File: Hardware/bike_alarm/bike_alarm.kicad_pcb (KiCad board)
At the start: 2 copper layers, 4 parts, among them Q1 Q_NMOS_DGS, Y1 Piezo Buzzer

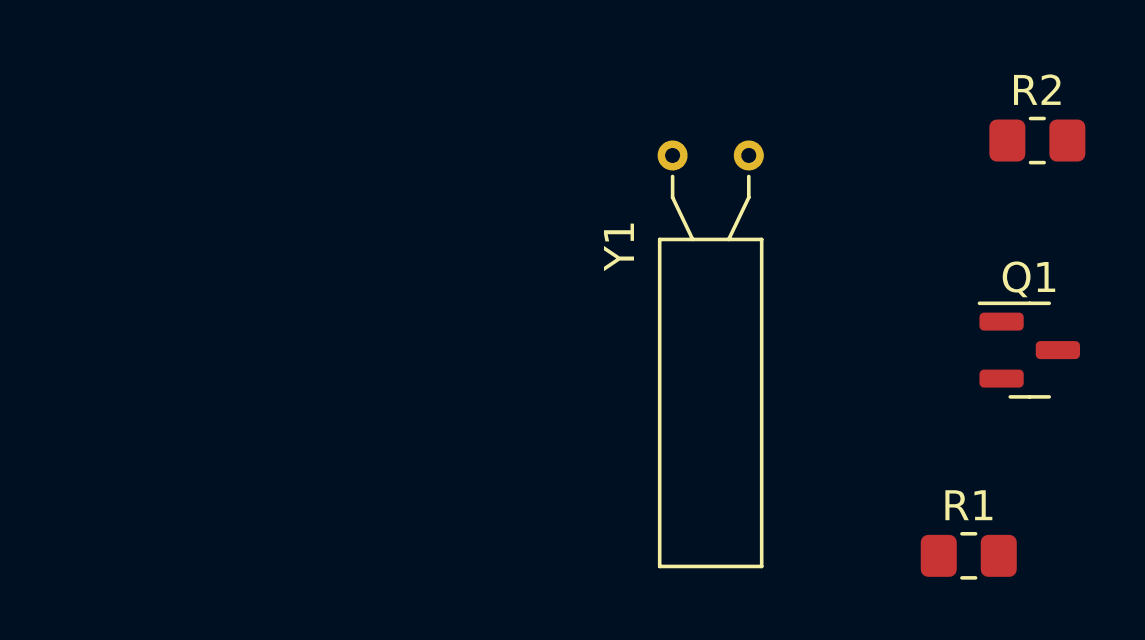
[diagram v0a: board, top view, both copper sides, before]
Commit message: bike_alarm pcb update and bom
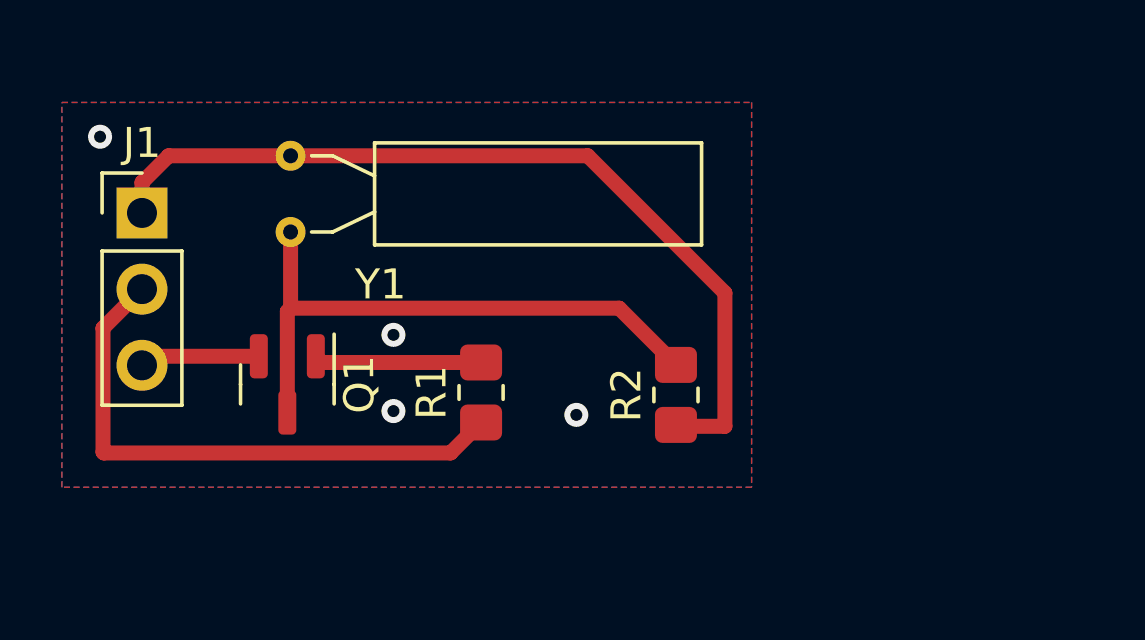
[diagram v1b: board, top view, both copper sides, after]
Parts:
- added J1: Conn_01x03_Male, Connector_PinHeader_2.54mm:PinHeader_1x03_P2.54mm_Vertical, F.Cu at (121.2, 81.4)
- Q1: value Q_NMOS_DGS -> Q_NMOS_GSD
- moved Q1 24.8 mm to (126.0, 87.1), turned to -90 degrees
- moved R1 17.1 mm to (132.5, 87.4), turned to 90 degrees
- moved R2 14.7 mm to (139.0, 87.5), turned to 90 degrees
- moved Y1 13.0 mm to (126.1, 82.0), turned to 90 degrees
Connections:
- Q1 pad 1: Net-(Y1-Pad1) -> Net-(R1-Pad2)
- Q1 pad 2: Net-(Q1-Pad2) -> GND
- Q1 pad 3: GND -> Net-(R2-Pad2)
- R1 pad 2: Net-(Q1-Pad2) -> Net-(R1-Pad2)
- R2 pad 2: Net-(Y1-Pad1) -> Net-(R2-Pad2)
- Y1 pad 1: Net-(Y1-Pad1) -> Net-(R2-Pad2)
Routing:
- net +3V3: track 0.00 -> 28.8 mm
- net Net-(R2-Pad2): track 0.00 -> 19.7 mm
- net /ALARM_CTRL: track 0.00 -> 19.0 mm
- net Net-(R1-Pad2): track 0.00 -> 5.59 mm
- net GND: track 0.00 -> 4.02 mm, vias 0 -> 4
- added copper zone on B.Cu, net GND
- added copper zone on F.Cu, net GND

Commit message: all boards pass DRC and have appropriate silkscreens, will order tomorrow
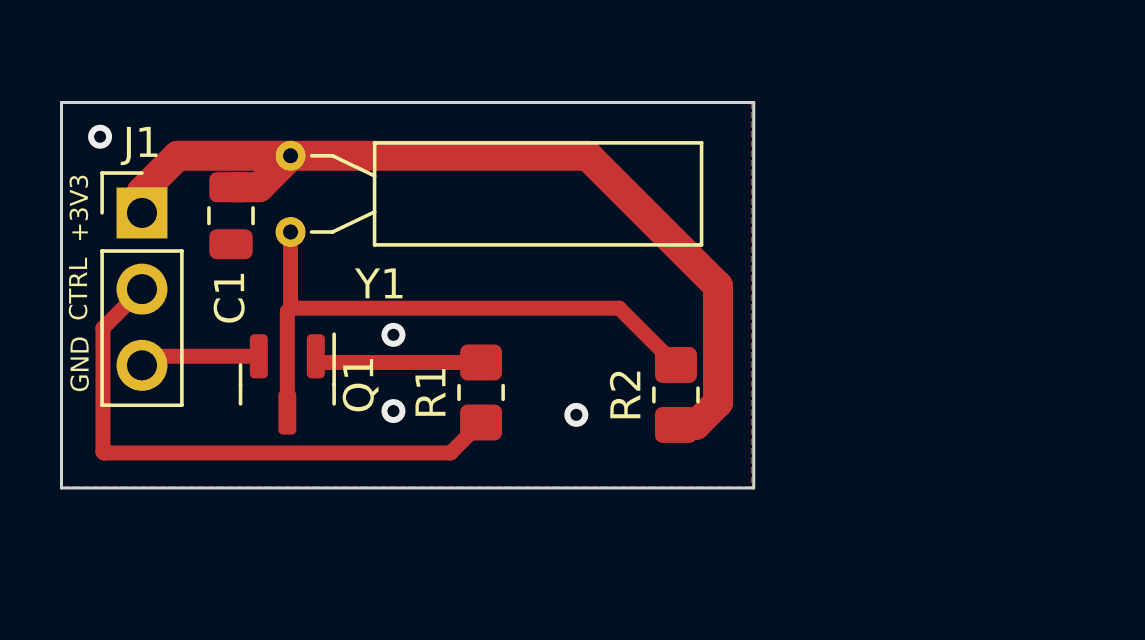
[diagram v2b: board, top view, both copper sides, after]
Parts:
- added C1: 1u, Capacitor_SMD:C_0805_2012Metric, F.Cu at (124.1, 81.5)
- R1: value R_US -> 15
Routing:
- net +3V3: track 28.8 -> 30.2 mm
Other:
- board outline added: 23.1 x 12.9 mm
- board text added: "+3V3"
- board text added: "Alarm Board ECE445 SP22 Group 45 v0.0.1"
- board text added: "CTRL"
- board text added: "GND"
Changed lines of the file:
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@@
   )
   (net 0 "")
-  (net 1 "Net-(R1-Pad2)")
+  (net 1 "Net-(Q1-Pad1)")
   (net 2 "GND")
   (net 3 "/ALARM_CTRL")
   (net 4 "+3V3")
-  (net 5 "Net-(R2-Pad2)")
+  (net 5 "Net-(Q1-Pad3)")
   (footprint "Resistor_SMD:R_0805_2012Metric_Pad1.20x1.40mm_HandSolder" (layer "F.Cu")
     (at 138.957 87.473 90)
@@
       (net 4 "+3V3") (pintype "passive"))
     (pad "2" smd roundrect (at 1 0 90) (size 1.2 1.4) (layers "F.Cu" "F.Paste" "F.Mask") (roundrect_rratio 0.208333)
-      (net 5 "Net-(R2-Pad2)") (pintype "passive"))
+      (net 5 "Net-(Q1-Pad3)") (pintype "passive"))
     (model "${KICAD6_3DMODEL_DIR}/Resistor_SMD.3dshapes/R_0805_2012Metric.wrl"
       (offset (xyz 0 0 0))
@@
       (effects (font (size 1 1) (thickness 0.15)))
     )
-    (fp_text value "R_US" (at 0 1.65 90) (layer "F.Fab")
+    (fp_text value "15" (at 0 1.65 90) (layer "F.Fab")
       (effects (font (size 1 1) (thickness 0.15)))
     )
@@
       (net 3 "/ALARM_CTRL") (pintype "passive"))
     (pad "2" smd roundrect (at 1 0 90) (size 1.2 1.4) (layers "F.Cu" "F.Paste" "F.Mask") (roundrect_rratio 0.208333)
-      (net 1 "Net-(R1-Pad2)") (pintype "passive"))
+      (net 1 "Net-(Q1-Pad1)") (pintype "passive"))
     (model "${KICAD6_3DMODEL_DIR}/Resistor_SMD.3dshapes/R_0805_2012Metric.wrl"
+      (offset (xyz 0 0 0))
+      (scale (xyz 1 1 1))
+      (rotate (xyz 0 0 0))
+    )
+  )
+  (footprint "Capacitor_SMD:C_0805_2012Metric" (layer "F.Cu")
+    (at 124.125 81.5 -90)
+    (descr "Capacitor SMD 0805 (2012 Metric), square (rectangular) end terminal, IPC_7351 nominal, (Body size source: IPC-SM-782 page 76, https://www.pcb-3d.com/wordpress/wp-content/uploads/ipc-sm-782a_amendment_1_and_2.pdf, https://docs.google.com/spreadsheets/d/1BsfQQcO9C6DZCsRaXUlFlo91Tg2WpOkGARC1WS5S8t0/edit?usp=sharing), generated with kicad-footprint-generator")
+    (tags "capacitor")
+    (property "Sheetfile" "bike_alarm.kicad_sch")
+    (property "Sheetname" "")
+    (attr smd)
+    (fp_text reference "C1" (at 2.725 0.025 90) (layer "F.SilkS")
+      (effects (font (size 1 1) (thickness 0.15)))
+    )
+    (fp_text value "1u" (at 0 1.68 90) (layer "F.Fab")
+      (effects (font (size 1 1) (thickness 0.15)))
+    )
+    (fp_text user "${REFERENCE}" (at 0 0 90) (layer "F.Fab")
+      (effects (font (size 0.5 0.5) (thickness 0.08)))
+    )
+    (fp_line (start -0.261252 -0.735) (end 0.261252 -0.735) (layer "F.SilkS") (width 0.12))
+    (fp_line (start -0.261252 0.735) (end 0.261252 0.735) (layer "F.SilkS") (width 0.12))
+    (fp_line (start -1.7 -0.98) (end 1.7 -0.98) (layer "F.CrtYd") (width 0.05))
+    (fp_line (start -1.7 0.98) (end -1.7 -0.98) (layer "F.CrtYd") (width 0.05))
+    (fp_line (start 1.7 0.98) (end -1.7 0.98) (layer "F.CrtYd") (width 0.05))
+    (fp_line (start 1.7 -0.98) (end 1.7 0.98) (layer "F.CrtYd") (width 0.05))
+    (fp_line (start 1 0.625) (end -1 0.625) (layer "F.Fab") (width 0.1))
+    (fp_line (start 1 -0.625) (end 1 0.625) (layer "F.Fab") (width 0.1))
+    (fp_line (start -1 -0.625) (end 1 -0.625) (layer "F.Fab") (width 0.1))
+    (fp_line (start -1 0.625) (end -1 -0.625) (layer "F.Fab") (width 0.1))
+    (pad "1" smd roundrect locked (at -0.95 0 270) (size 1 1.45) (layers "F.Cu" "F.Paste" "F.Mask") (roundrect_rratio 0.25)
+      (net 4 "+3V3") (pintype "passive"))
+    (pad "2" smd roundrect locked (at 0.95 0 270) (size 1 1.45) (layers "F.Cu" "F.Paste" "F.Mask") (roundrect_rratio 0.25)
+      (net 2 "GND") (pintype "passive"))
+    (model "${KICAD6_3DMODEL_DIR}/Capacitor_SMD.3dshapes/C_0805_2012Metric.wrl"
       (offset (xyz 0 0 0))
       (scale (xyz 1 1 1))
@@
     (fp_line (start 0.65 1.45) (end -0.65 1.45) (layer "F.Fab") (width 0.1))
     (pad "1" smd roundrect (at -0.9375 -0.95 270) (size 1.475 0.6) (layers "F.Cu" "F.Paste" "F.Mask") (roundrect_rratio 0.25)
-      (net 1 "Net-(R1-Pad2)") (pinfunction "G") (pintype "input"))
+      (net 1 "Net-(Q1-Pad1)") (pinfunction "G") (pintype "input"))
     (pad "2" smd roundrect (at -0.9375 0.95 270) (size 1.475 0.6) (layers "F.Cu" "F.Paste" "F.Mask") (roundrect_rratio 0.25)
       (net 2 "GND") (pinfunction "S") (pintype "passive"))
     (pad "3" smd roundrect (at 0.9375 0 270) (size 1.475 0.6) (layers "F.Cu" "F.Paste" "F.Mask") (roundrect_rratio 0.25)
-      (net 5 "Net-(R2-Pad2)") (pinfunction "D") (pintype "passive"))
+      (net 5 "Net-(Q1-Pad3)") (pinfunction "D") (pintype "passive"))
     (model "${KICAD6_3DMODEL_DIR}/Package_TO_SOT_SMD.3dshapes/SOT-23.wrl"
       (offset (xyz 0 0 0))
@@
     (fp_line (start 2.77 3) (end -0.23 3) (layer "F.Fab") (width 0.1))
     (pad "1" thru_hole circle (at 0 0 90) (size 1 1) (drill 0.5) (layers *.Cu *.Mask)
-      (net 5 "Net-(R2-Pad2)") (pinfunction "1") (pintype "passive"))
+      (net 5 "Net-(Q1-Pad3)") (pinfunction "1") (pintype "passive"))
     (pad "2" thru_hole circle (at 2.54 0 90) (size 1 1) (drill 0.5) (layers *.Cu *.Mask)
       (net 4 "+3V3") (pinfunction "2") (pintype "passive"))
@@
       (rotate (xyz 0 0 0))
     )
+  )
+  (gr_rect (start 118.475 77.725) (end 141.55 90.575) (layer "Edge.Cuts") (width 0.1) (fill none))
+  (gr_text "Alarm Board\nECE445 SP22\nGroup 45\nv0.0.1" (at 134.925 82.325) (layer "B.SilkS")
+    (effects (font (size 1 1) (thickness 0.15)) (justify mirror))
+  )
+  (gr_text "+3V3" (at 119.075 81.25 90) (layer "F.SilkS")
+    (effects (font (size 0.6 0.6) (thickness 0.15)))
+  )
+  (gr_text "CTRL" (at 119.05 83.95 90) (layer "F.SilkS")
+    (effects (font (size 0.6 0.6) (thickness 0.15)))
+  )
+  (gr_text "GND" (at 119.1 86.45 90) (layer "F.SilkS")
+    (effects (font (size 0.6 0.6) (thickness 0.15)))
+  )
+  (dimension (type aligned) (layer "Dwgs.User")
+    (pts (xy 118.475 77.725) (xy 141.55 77.725))
+    (height -1.8)
+    (gr_text "23.0750 mm" (at 130.0125 74.775) (layer "Dwgs.User")
+      (effects (font (size 1 1) (thickness 0.15)))
+    )
+    (format (units 3) (units_format 1) (precision 4))
+    (style (thickness 0.15) (arrow_length 1.27) (text_position_mode 0) (extension_height 0.58642) (extension_offset 0.5) keep_text_aligned)
+  )
+  (dimension (type aligned) (layer "Dwgs.User")
+    (pts (xy 141.525 77.725) (xy 141.55 90.575))
+    (height -1.400191)
+    (gr_text "12.8500 mm" (at 144.087686 84.145039 270.1114702) (layer "Dwgs.User")
+      (effects (font (size 1 1) (thickness 0.15)))
+    )
+    (format (units 3) (units_format 1) (precision 4))
+    (style (thickness 0.15) (arrow_length 1.27) (text_position_mode 0) (extension_height 0.58642) (extension_offset 0.5) keep_text_aligned)
   )
   (segment (start 127.1605 86.392) (end 126.953 86.1845) (width 0.5) (layer "F.Cu") (net 1))
@@
   (segment (start 131.445 89.408) (end 132.461 88.392) (width 0.5) (layer "F.Cu") (net 3))
   (segment (start 119.858489 85.246511) (end 119.858489 89.378489) (width 0.5) (layer "F.Cu") (net 3))
-  (segment (start 139.003 88.519) (end 138.957 88.473) (width 0.5) (layer "F.Cu") (net 4))
-  (segment (start 122.047 79.502) (end 126.111 79.502) (width 0.5) (layer "F.Cu") (net 4))
-  (segment (start 140.589 84.074) (end 140.589 88.519) (width 0.5) (layer "F.Cu") (net 4))
-  (segment (start 136.017 79.502) (end 140.589 84.074) (width 0.5) (layer "F.Cu") (net 4))
-  (segment (start 121.158 81.407) (end 121.158 80.391) (width 0.5) (layer "F.Cu") (net 4))
-  (segment (start 140.589 88.519) (end 139.003 88.519) (width 0.5) (layer "F.Cu") (net 4))
-  (segment (start 126.111 79.502) (end 136.017 79.502) (width 0.5) (layer "F.Cu") (net 4))
-  (segment (start 121.158 80.391) (end 122.047 79.502) (width 0.5) (layer "F.Cu") (net 4))
+  (segment (start 140.35652 83.84152) (end 140.35652 87.73148) (width 1) (layer "F.Cu") (net 4))
+  (segment (start 126.111 79.502) (end 136.017 79.502) (width 1) (layer "F.Cu") (net 4))
+  (segment (start 121.158 80.692) (end 122.348 79.502) (width 1) (layer "F.Cu") (net 4))
+  (segment (start 139.615 88.473) (end 138.957 88.473) (width 1) (layer "F.Cu") (net 4))
+  (segment (start 124.125 80.55) (end 125.063 80.55) (width 1) (layer "F.Cu") (net 4))
+  (segment (start 126.111 79.502) (end 122.348 79.502) (width 1) (layer "F.Cu") (net 4))
+  (segment (start 121.158 81.407) (end 121.158 80.692) (width 1) (layer "F.Cu") (net 4))
+  (segment (start 140.35652 87.73148) (end 139.615 88.473) (width 1) (layer "F.Cu") (net 4))
+  (segment (start 125.063 80.55) (end 126.111 79.502) (width 1) (layer "F.Cu") (net 4))
+  (segment (start 136.017 79.502) (end 140.35652 83.84152) (width 1) (layer "F.Cu") (net 4))
   (segment (start 126.003 88.0595) (end 126.003 84.69) (width 0.5) (layer "F.Cu") (net 5))
   (segment (start 126.003 84.69) (end 126.111 84.582) (width 0.5) (layer "F.Cu") (net 5))
